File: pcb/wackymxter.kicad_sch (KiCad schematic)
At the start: 72 parts, among them J1 OLED_128x32, U1 Arduino_Pro_Micro

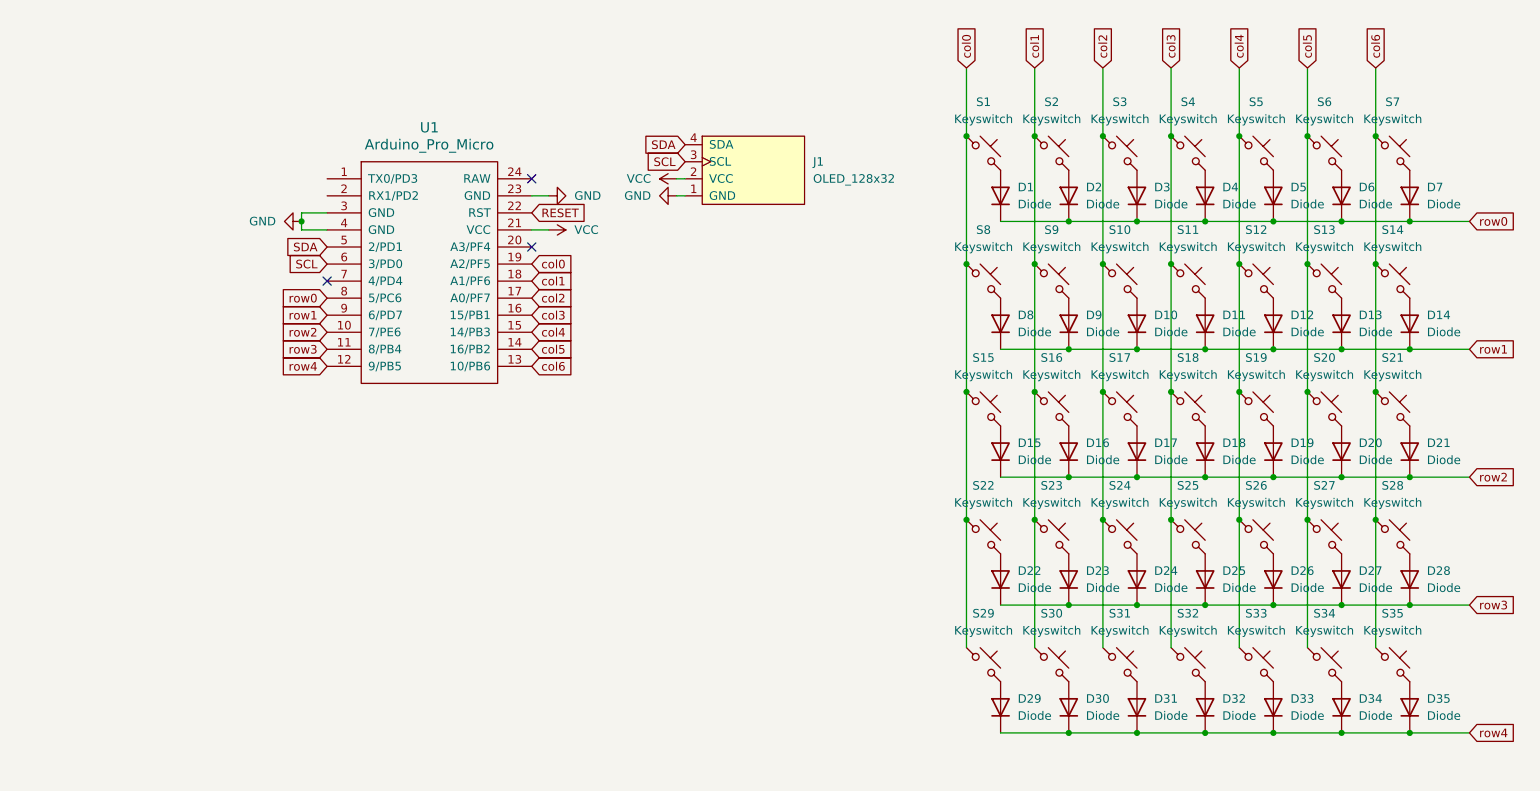
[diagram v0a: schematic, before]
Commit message: [KiCAD] switch to RP2040
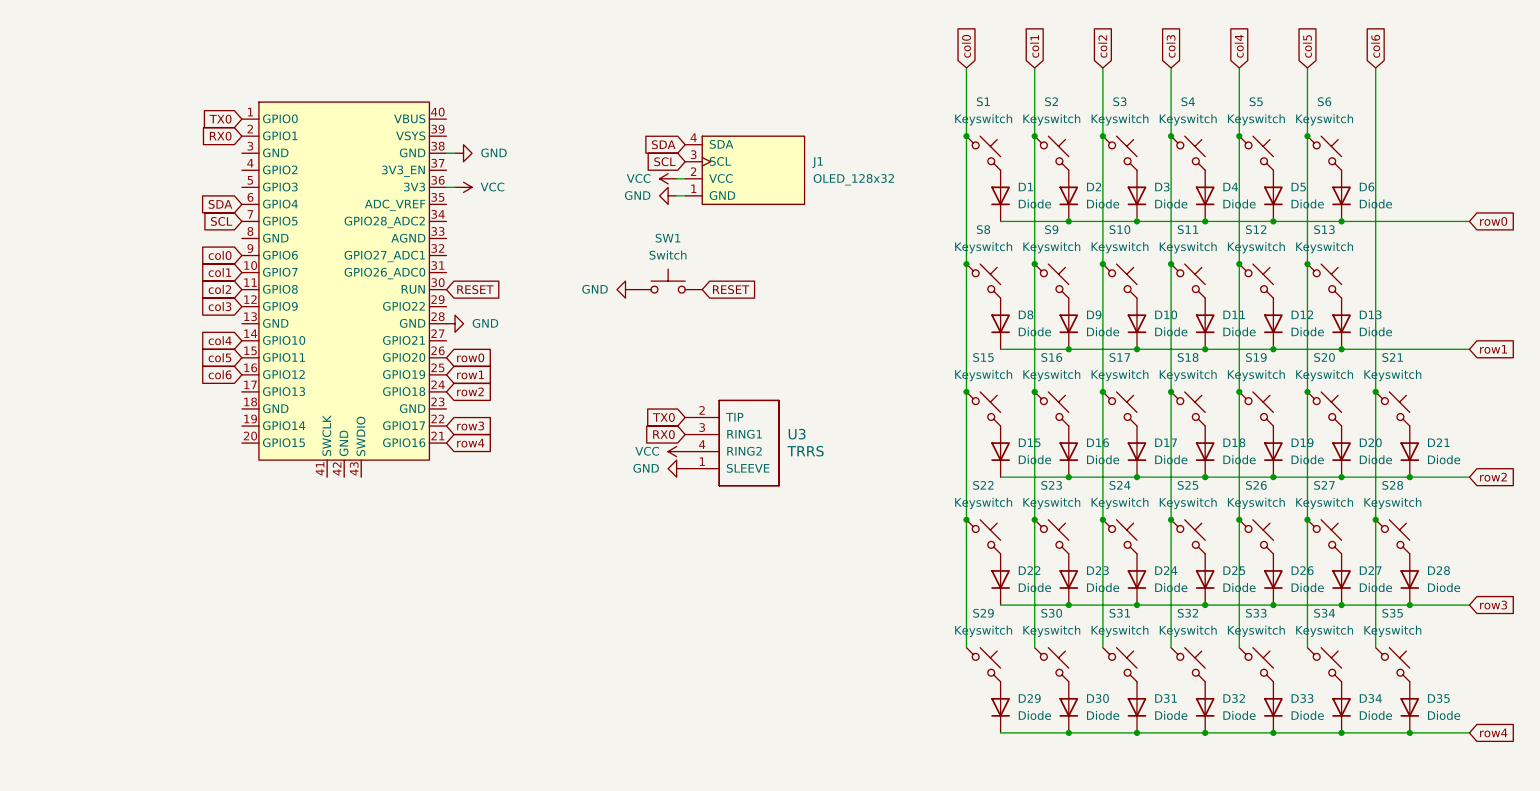
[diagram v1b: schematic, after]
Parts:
- removed D14, D7: Diode, ScottoKeebs_Components:Diode_DO-35, symbol ScottoKeebs:Placeholder_Diode
- removed S14, S7: Keyswitch, ScottoKeebs_MX:MX_PCB_1.00u, symbol ScottoKeebs:Placeholder_Keyswitch
- removed U1: Arduino_Pro_Micro, ScottoKeebs_MCU:Arduino_Pro_Micro, symbol ScottoKeebs:MCU_Arduino_Pro_Micro
- added SW1: Switch, Button_Switch_SMD:SW_Push_1P1T_NO_CK_KMR2, symbol ScottoKeebs:Placeholder_Switch
- added U2: Raspberry_Pi_Pico, ScottoKeebs_MCU:Raspberry_Pi_Pico, symbol ScottoKeebs:MCU_Raspberry_Pi_Pico
- added U3: TRRS, ScottoKeebs_Components:TRRS_PJ-320A, symbol ScottoKeebs:Placeholder_TRRS
- S33: footprint ScottoKeebs_MX:MX_PCB_1.00u -> ScottoKeebs_MX:MX_PCB_1.50u
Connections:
- net GND: now also SW1.1, U2.28 (GND), U2.38 (GND), U3.1 (SLEEVE)
- net RESET: now also SW1.2, U2.30 (RUN)
- net SCL: now also U2.7 (GPIO5)
- net SDA: now also U2.6 (GPIO4)
- net VCC: now also U2.36 (3V3), U3.4 (RING2)
- net col0: now also U2.9 (GPIO6)
- net col1: now also U2.10 (GPIO7)
- net col2: now also U2.11 (GPIO8)
- net col3: now also U2.12 (GPIO9)
- net col4: now also U2.14 (GPIO10)
- net col5: now also U2.15 (GPIO11)
- net col6: now also U2.16 (GPIO12)
- net row0: now also U2.26 (GPIO20)
- net row1: now also U2.25 (GPIO19)
- net row2: now also U2.24 (GPIO18)
- net row3: now also U2.22 (GPIO17)
- net row4: now also U2.21 (GPIO16)
- new net RX0: U2.2 (GPIO1), U3.3 (RING1)
- new net TX0: U2.1 (GPIO0), U3.2 (TIP)
- no-connect marks 3 -> 0

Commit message: [KiCAD] V0.1: fully connected pcb
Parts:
- removed D35: Diode, ScottoKeebs_Components:Diode_DO-35, symbol ScottoKeebs:Placeholder_Diode
- removed S35: Keyswitch, ScottoKeebs_MX:MX_PCB_1.00u, symbol ScottoKeebs:Placeholder_Keyswitch
- removed SW1: Switch, Button_Switch_SMD:SW_Push_1P1T_NO_CK_KMR2, symbol ScottoKeebs:Placeholder_Switch
- added D14, D7: Diode, ScottoKeebs_Components:Diode_DO-35, symbol ScottoKeebs:Placeholder_Diode
- added R1, R2: Resistor, Resistor_THT:R_Axial_DIN0204_L3.6mm_D1.6mm_P5.08mm_Horizontal, symbol ScottoKeebs:Placeholder_Resistor
- added S14, S7: Keyswitch, ScottoKeebs_MX:MX_PCB_1.00u, symbol ScottoKeebs:Placeholder_Keyswitch
- added U1: RP2040_Zero, ScottoKeebs_MCU:RP2040_Zero, symbol ScottoKeebs:MCU_RP2040_Zero
- S33: footprint ScottoKeebs_MX:MX_PCB_1.50u -> ScottoKeebs_MX:MX_PCB_1.00u
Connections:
- net GND: now also U1.22 (GND); no longer U2.28 (GND), U2.38 (GND)
- net RX0: now also U3.4 (RING2), R2.2, U1.2 (1); no longer U2.2 (GPIO1), U3.3 (RING1)
- net SCL: now also U1.4 (3); no longer U2.7 (GPIO5)
- net SDA: now also U1.3 (2); no longer U2.6 (GPIO4)
- net TX0: now also U3.3 (RING1), R1.2, U1.1 (0); no longer U2.1 (GPIO0), U3.2 (TIP)
- net VCC: now also U3.2 (TIP), R1.1, R2.1, U1.21 (3V3); no longer U2.36 (3V3), U3.4 (RING2)
- net col0: now also U1.5 (4); no longer U2.9 (GPIO6)
- net col1: now also U1.6 (5); no longer U2.10 (GPIO7)
- net col2: now also U1.7 (6); no longer U2.11 (GPIO8)
- net col3: now also U1.20 (29); no longer U2.12 (GPIO9)
- net col4: now also U1.19 (28); no longer U2.14 (GPIO10)
- net col5: now also U1.18 (27); no longer U2.15 (GPIO11)
- net col6: now also S14.1, S7.1, U1.17 (26); no longer U2.16 (GPIO12)
- net row0: now also D7.1 (K), U1.10 (9); no longer U2.26 (GPIO20)
- net row1: now also D14.1 (K), U1.11 (10); no longer U2.25 (GPIO19)
- net row2: now also U1.12 (11); no longer U2.24 (GPIO18)
- net row3: now also U1.13 (12); no longer U2.22 (GPIO17)
- net row4: now also U1.14 (13); no longer U2.21 (GPIO16)
- net RESET: no longer names the net of U2.30 (RUN)
- new net: D14.2 (A), S14.2
- new net: D7.2 (A), S7.2
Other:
- moved on the sheet: J1, U3
